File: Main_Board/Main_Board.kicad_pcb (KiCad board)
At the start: 2 copper layers, 99 x 70 mm, 28 parts, among them J1 DB25, P1 CONN_01X08, P2 CONN_01X08, P3 CONN_01X03, U1 TLV1117LV33, U2 DYS_mini_ESC, U3 DYS_mini_ESC, U4 DYS_mini_ESC, U5 DYS_mini_ESC, U6 TENDA_P200, U7 AL8805W5

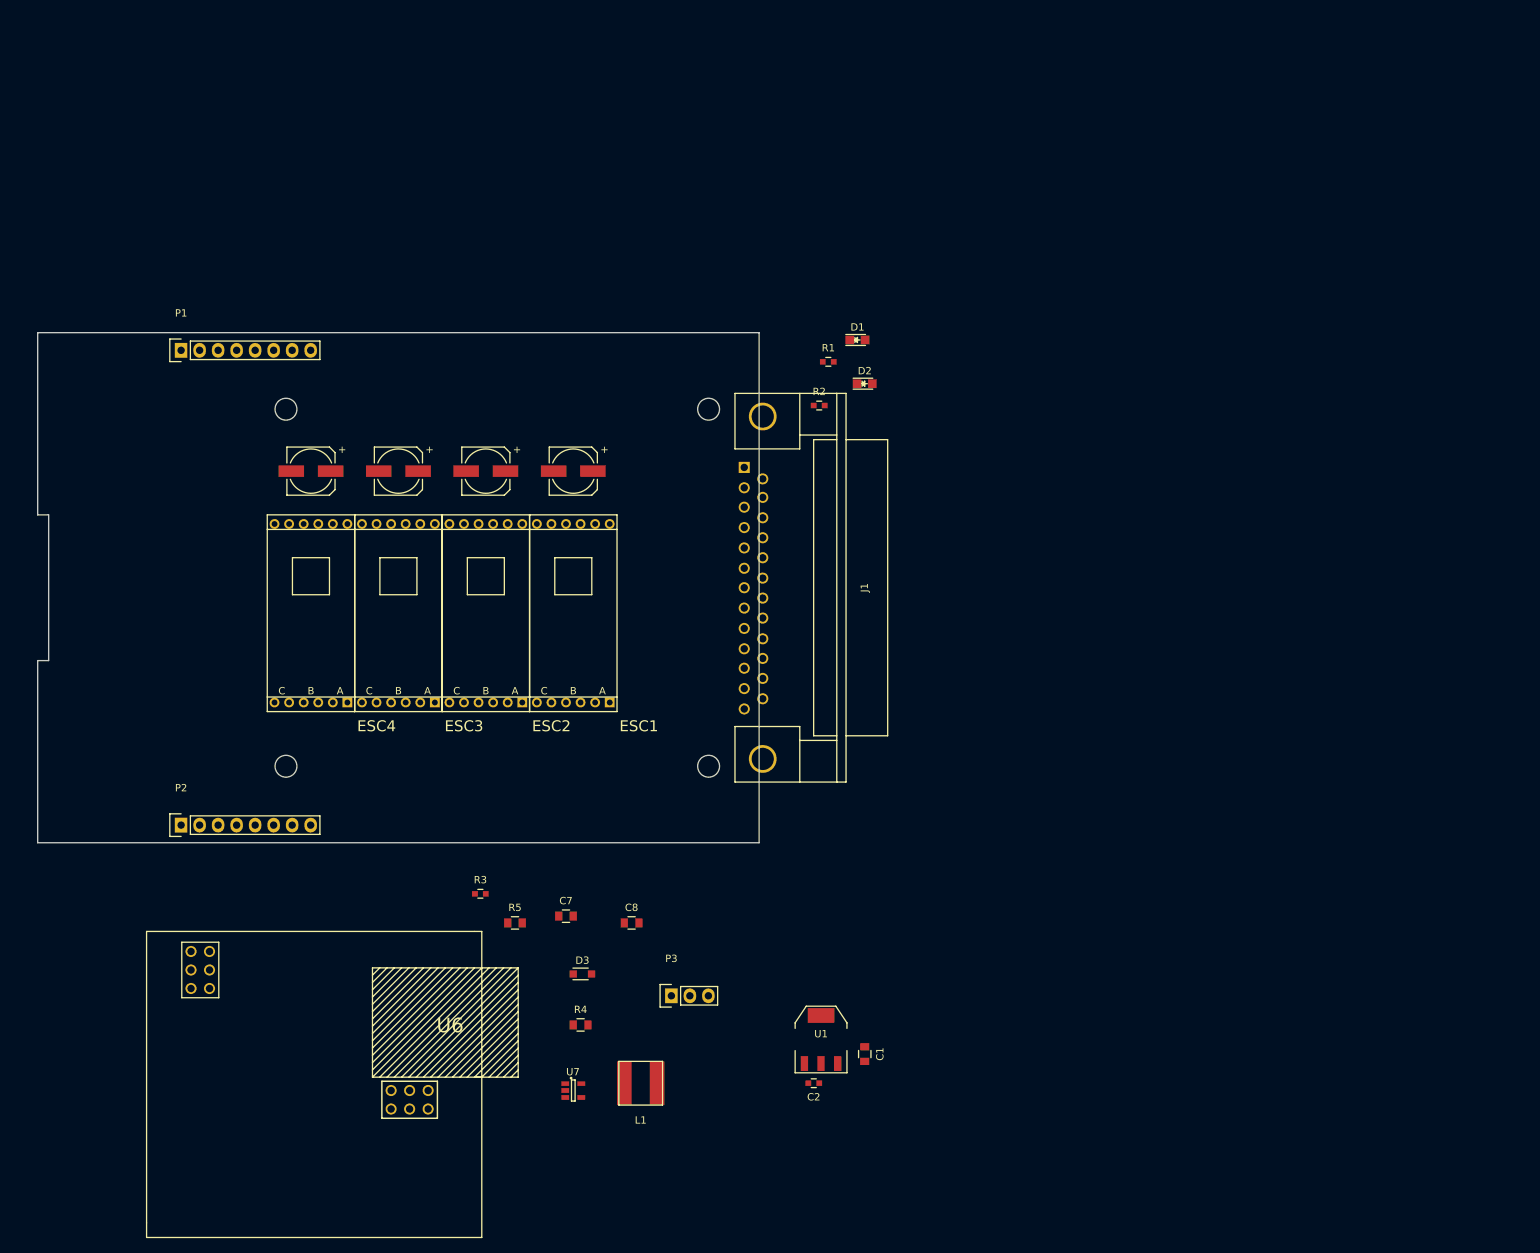
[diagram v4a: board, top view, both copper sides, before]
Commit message: Main Board : Recover LED driver USB Dist Board : Delete ADC voltage divider
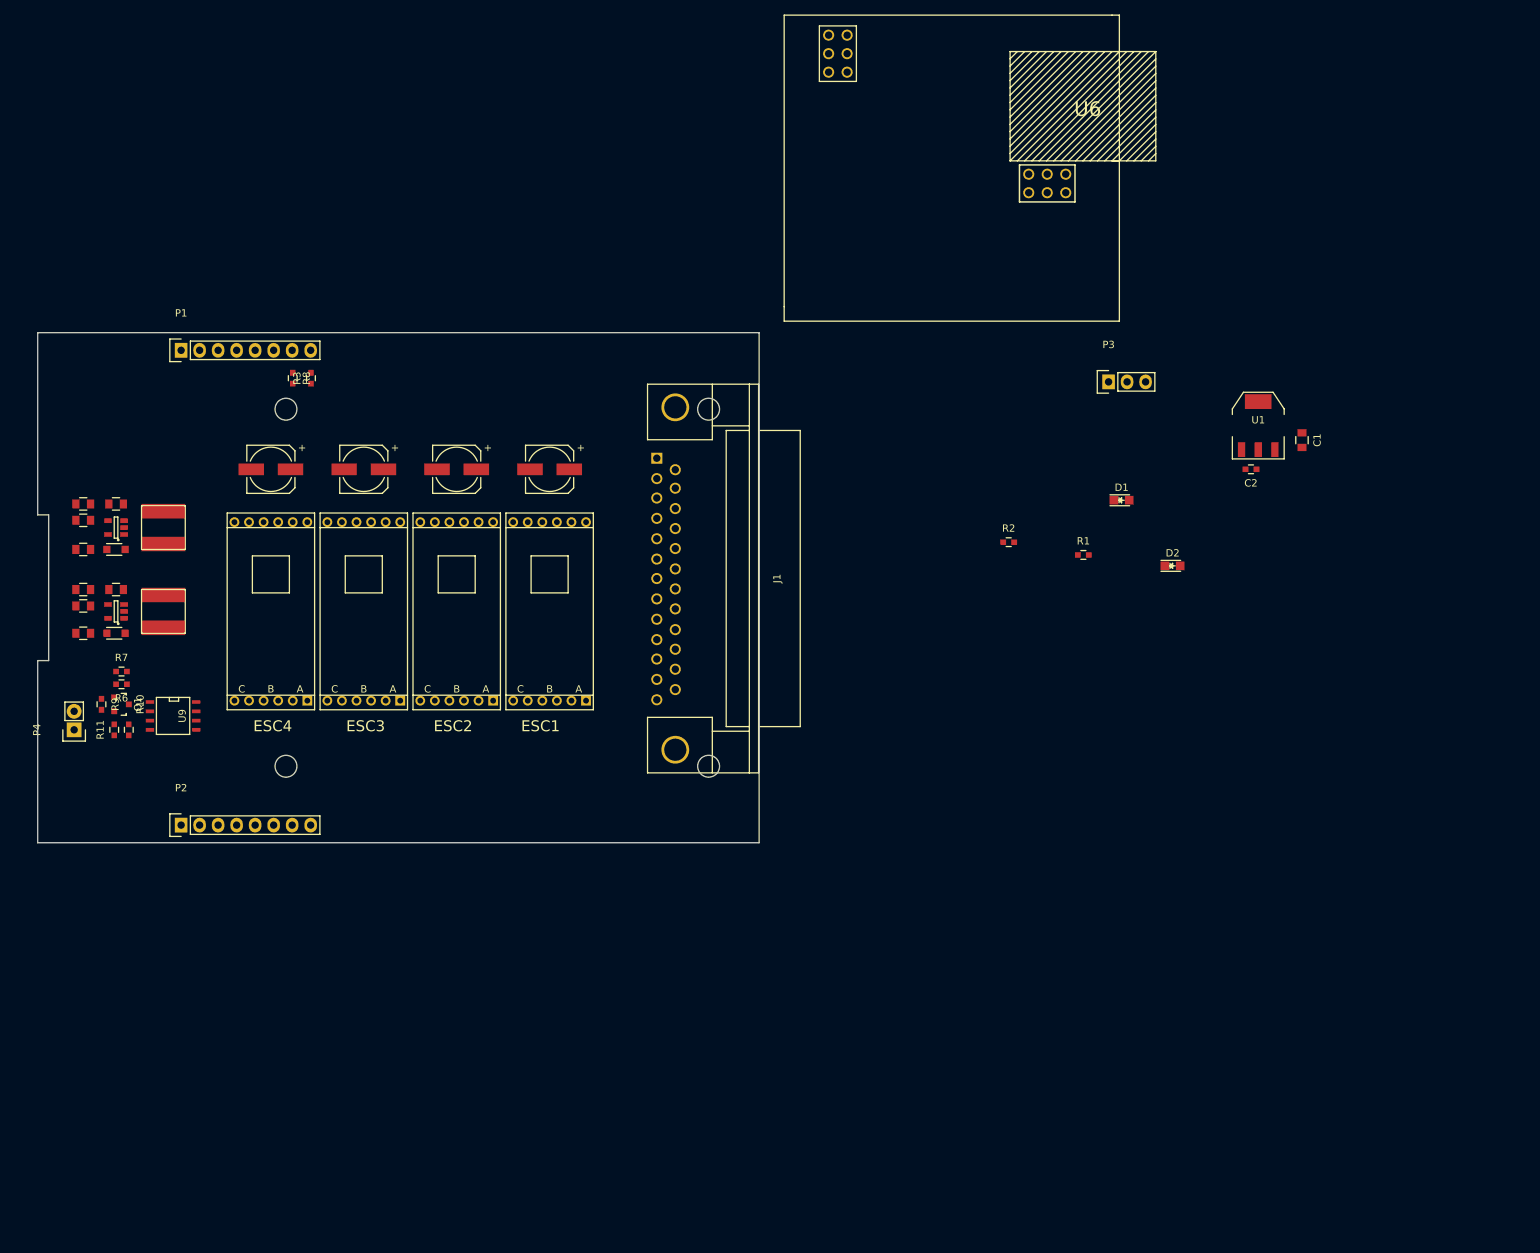
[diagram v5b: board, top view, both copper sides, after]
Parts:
- added C10: 2.2uF, Capacitors_SMD:C_0805, F.Cu at (56.8, 106.2)
- added C9: 1uF, Capacitors_SMD:C_0805, F.Cu at (61.2, 100.2)
- added D4: BAT20JFILM, Diodes_SMD:SOD-323_HandSoldering, F.Cu at (61.2, 106.2)
- added L2: 33uH, KiCad_Footprint:inductor_33uH, F.Cu at (67.8, 103.2)
- added P4: CONN_01X02, Socket_Strips:Socket_Strip_Straight_1x02, F.Cu at (55.5, 119.5)
- added Q1: DMN65D8L, TO_SOT_Packages_SMD:SOT-23, F.Cu at (62.0, 116.0)
- added R10: 10k, Capacitors_SMD:C_0603, F.Cu at (63.0, 119.5)
- added R11: 1k, Capacitors_SMD:C_0603, F.Cu at (61.0, 119.5)
- added R12: 0.5, Capacitors_SMD:C_0805, F.Cu at (56.8, 102.5)
- added R13: 0.5, Capacitors_SMD:C_0805, F.Cu at (56.8, 100.2)
- added R6: 20k 1%, Capacitors_SMD:C_0603, F.Cu at (62.0, 113.2)
- added R7: 102k 1%, Capacitors_SMD:C_0603, F.Cu at (62.0, 111.5)
- added R8: 10k, Capacitors_SMD:C_0603, F.Cu at (85.5, 71.2)
- added R9: 10k, Capacitors_SMD:C_0603, F.Cu at (59.2, 116.0)
- added U8: AL8805W5, TO_SOT_Packages_SMD:SOT-23-5, F.Cu at (61.2, 103.2)
- added U9: SI4425DDY, SMD_Packages:SOIC-8-N, F.Cu at (69.1, 117.6)
- moved U6 153.2 mm to (175.4, 42.4)
- moved C1 103.4 mm to (224.0, 79.8)
- moved C2 103.4 mm to (217.0, 83.8)
- moved P3 103.4 mm to (197.5, 71.8)
- moved U1 103.4 mm to (218.0, 77.8)
- moved L1 100.5 mm to (67.8, 91.8), turned to 90 degrees
- moved U7 99.5 mm to (61.2, 91.8), turned to 180 degrees
- moved R4 98.8 mm to (56.8, 88.5)
- moved C8 91.0 mm to (56.8, 94.8), turned to 180 degrees
- moved D3 86.5 mm to (61.2, 94.8)
- moved C7 83.7 mm to (61.2, 88.5)
- moved R5 81.0 mm to (56.8, 90.8)
- moved R3 74.5 mm to (88.0, 71.2), turned to 90 degrees
- moved D2 49.1 mm to (206.2, 97.0)
- moved R1 43.9 mm to (194.0, 95.5)
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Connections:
- net /Bottom_Board/LED+ renamed /Bottom_Board/LED1+
- net /Bottom_Board/LED- renamed /Bottom_Board/LED1-
- C3 pad 1: /Bottom_Board/V_BAT -> /Bottom_Board/V_PWR
- C4 pad 1: /Bottom_Board/V_BAT -> /Bottom_Board/V_PWR
- C5 pad 1: /Bottom_Board/V_BAT -> /Bottom_Board/V_PWR
- C6 pad 1: /Bottom_Board/V_BAT -> /Bottom_Board/V_PWR
- C8 pad 1: /Bottom_Board/V_BAT -> /Bottom_Board/V_PWR
- D3 pad 1: /Bottom_Board/V_BAT -> /Bottom_Board/V_PWR
- P1 pad 7: (no net) -> /Bottom_Board/CH6
- P2 pad 1: (no net) -> /Bottom_Board/ADC
- P2 pad 6: (no net) -> /Bottom_Board/SW
- R4 pad 1: /Bottom_Board/V_BAT -> /Bottom_Board/V_PWR
- R5 pad 1: /Bottom_Board/V_BAT -> /Bottom_Board/V_PWR
- U2 pad 3: /Bottom_Board/V_BAT -> /Bottom_Board/V_PWR
- U3 pad 3: /Bottom_Board/V_BAT -> /Bottom_Board/V_PWR
- U4 pad 3: /Bottom_Board/V_BAT -> /Bottom_Board/V_PWR
- U5 pad 3: /Bottom_Board/V_BAT -> /Bottom_Board/V_PWR
- U7 pad 5: /Bottom_Board/V_BAT -> /Bottom_Board/V_PWR

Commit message: development start
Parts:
- added C11: C, Capacitors_SMD:C_0805, F.Cu at (123.6, 131.9)
- added C12: C, Capacitors_SMD:C_0603, F.Cu at (125.8, 129.8)
- added P5: CONN_01X02, Socket_Strips:Socket_Strip_Straight_1x02, F.Cu at (119.6, 130.0)
- added R14: 10k, Capacitors_SMD:C_0603, B.Cu at (77.8, 70.9)
- added R15: 10k, Capacitors_SMD:C_0603, B.Cu at (75.3, 70.9)
- added R16: 10k, Capacitors_SMD:C_0603, B.Cu at (82.9, 70.9)
- added R17: 10k, Capacitors_SMD:C_0603, B.Cu at (80.4, 70.9)
- added U10: DSN-MINI-360, KiCad_Footprint:DSN-MINI-360, F.Cu at (106.7, 127.6)
- added U11: TLV1117LV33, TO_SOT_Packages_SMD:SOT-223, F.Cu at (131.6, 130.8)
- R3, R8: moved to B.Cu
- moved U2 2.00 mm to (120.8, 101.2)
- moved U3 2.00 mm to (108.0, 101.2)
- moved U4 2.00 mm to (95.2, 101.2)
- moved U5 2.00 mm to (82.5, 101.2)
- moved J1 1.26 mm to (136.7, 100.0)
- moved C3 1.00 mm to (120.8, 82.8)
- moved C4 1.00 mm to (108.0, 82.8)
- moved C5 1.00 mm to (95.2, 82.8)
- moved C6 1.00 mm to (82.5, 82.8)
- moved R3 0.35 mm to (88.0, 70.9)
- moved R8 0.35 mm to (85.5, 70.9)
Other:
- net class Default: trace_width 0.25 -> 2

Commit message: shit
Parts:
- added C13: 33uF, Capacitors_SMD:C_0603, F.Cu at (70.4, 99.5)
- added C14: 33uF, Capacitors_SMD:C_0603, F.Cu at (73.5, 99.5)
- added C15: 1uF, Capacitors_SMD:C_0603, B.Cu at (70.2, 108.8)
- added C16: 1uF, Capacitors_SMD:C_0603, B.Cu at (70.2, 105.7)
- added C17: 1uF, Capacitors_SMD:C_0603, B.Cu at (72.8, 108.8)
- added C18: 1uF, Capacitors_SMD:C_0603, B.Cu at (72.8, 105.7)
- added C19: 47pF, Capacitors_SMD:C_0603, F.Cu at (70.7, 114.8)
- added C20: 47pF, Capacitors_SMD:C_0603, F.Cu at (73.9, 114.8)
- added C21: 10uF, Capacitors_SMD:C_0603, F.Cu at (65.1, 95.2)
- added D5: LED, LEDs:LED_0805, F.Cu at (200.7, 154.0)
- added P10: CONN_01X02, Socket_Strips:Socket_Strip_Straight_1x02, F.Cu at (127.7, 76.5)
- added P11: CONN_01X02, Socket_Strips:Socket_Strip_Straight_1x02, F.Cu at (129.2, 123.5)
- added P12: CONN_01X02, Socket_Strips:Socket_Strip_Straight_1x02, F.Cu at (88.7, 123.5)
- added P13: CONN_02X07, Socket_Strips:Socket_Strip_Straight_2x07, F.Cu at (64.8, 123.2)
- added P14: USB_A, Connect:USB_Mini-B, F.Cu at (56.2, 130.4)
- added P6: BOOT, Socket_Strips:Socket_Strip_Straight_1x02, F.Cu at (214.2, 155.8)
- added P7: CONN_01X06, Socket_Strips:Socket_Strip_Straight_1x06, F.Cu at (53.5, 83.6)
- added P8: CONN_01X04, Socket_Strips:Socket_Strip_Angled_1x04, F.Cu at (57.5, 112.7)
- added P9: CONN_01X02, Socket_Strips:Socket_Strip_Straight_1x02, F.Cu at (89.5, 76.5)
- added Q2: BSS84, TO_SOT_Packages_SMD:SOT-23, F.Cu at (77.5, 117.5)
- added Q3: BSS138, TO_SOT_Packages_SMD:SOT-23, F.Cu at (60.3, 107.2)
- added Q4: BSS138, TO_SOT_Packages_SMD:SOT-23, F.Cu at (60.3, 103.8)
- added R18: 330, Capacitors_SMD:C_0603, F.Cu at (198.7, 154.1)
- added R19: 10k, Capacitors_SMD:C_0603, F.Cu at (205.5, 149.6)
- added R20: 10k, Capacitors_SMD:C_0603, F.Cu at (208.2, 156.6)
- added R21: 10k, Capacitors_SMD:C_0603, F.Cu at (77.5, 114.8)
- added R22: 1.5k, Capacitors_SMD:C_0603, F.Cu at (74.8, 117.5)
- added R23: 22, Capacitors_SMD:C_0603, F.Cu at (71.5, 117.5)
- added R24: 22, Capacitors_SMD:C_0603, F.Cu at (73.2, 117.5)
- added RP1: 220X4, Resistors_SMD:R_Array_Concave_4x0603, F.Cu at (58.4, 88.3)
- added RP2: 220X4, Resistors_SMD:R_Array_Concave_4x0603, F.Cu at (54.6, 88.2)
- added RP3: 220X4, Resistors_SMD:R_Array_Concave_4x0603, F.Cu at (55.0, 100.0)
- added SW1: RESET, KiCad_Footprint:smd_push, F.Cu at (214.9, 148.9)
- added U12: STM32F103CBT6, Housings_QFP:LQFP-48_7x7mm_Pitch0.5mm, F.Cu at (71.4, 107.3)
- added U13: pca9685, Housings_SSOP:TSSOP-28_4.4x9.7mm_Pitch0.65mm, F.Cu at (58.1, 93.9)
- added X1: 8MHz, KiCad_Footprint:crystal_maple, F.Cu at (72.0, 96.5)
- P1, P2: value CONN_01X08 -> CONN_01X06; footprint Socket_Strips:Socket_Strip_Straight_1x08 -> Socket_Strips:Socket_Strip_Straight_1x06
- R14, R15, R16, R17, R3, R8: moved to F.Cu
- moved P4 79.8 mm to (117.0, 68.7), turned to 270 degrees
- moved U6 75.0 mm to (221.5, 101.5)
- moved R11 71.6 mm to (111.5, 68.7), turned to 270 degrees
- moved R9 69.5 mm to (113.2, 72.2), turned to 90 degrees
- moved R10 68.9 mm to (109.5, 68.7), turned to 90 degrees
- moved Q1 65.3 mm to (110.4, 72.2), turned to 90 degrees
- moved R6 61.8 mm to (110.5, 74.9), turned to 0 degrees
- moved R7 59.7 mm to (110.5, 76.7), turned to 180 degrees
- moved U9 58.2 mm to (103.4, 70.6), turned to 90 degrees
- moved P2 50.9 mm to (56.4, 83.6), turned to 90 degrees
- moved C1 47.7 mm to (251.5, 40.8)
- moved C2 47.7 mm to (244.5, 44.8)
- moved D1 47.7 mm to (226.8, 49.0)
- moved D2 47.7 mm to (233.8, 58.0)
- moved R1 47.7 mm to (221.5, 56.5)
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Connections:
- C10 pad 2: /Bottom_Board/L_GND -> GNDPWR
- C11 pad 2: GND -> GNDD
- C12 pad 2: GND -> GNDD
- C3 pad 2: /Bottom_Board/L_GND -> GNDPWR
- C4 pad 2: /Bottom_Board/L_GND -> GNDPWR
- C5 pad 2: /Bottom_Board/L_GND -> GNDPWR
- C6 pad 2: /Bottom_Board/L_GND -> GNDPWR
- C8 pad 2: /Bottom_Board/L_GND -> GNDPWR
- P1 pad 1: /Bottom_Board/V_BAT -> Net-(P1-Pad1)
- P1 pad 2: /Bottom_Board/L_GND -> Net-(P1-Pad2)
- P1 pad 3: /Bottom_Board/CH2 -> Net-(P1-Pad3)
- P1 pad 4: /Bottom_Board/CH1 -> Net-(P1-Pad4)
- P1 pad 5: /Bottom_Board/CH4 -> Net-(P1-Pad5)
- P1 pad 6: /Bottom_Board/CH3 -> Net-(P1-Pad6)
- P2 pad 1: /Bottom_Board/ADC -> /Bottom_Board/5V
- P2 pad 2: /Bottom_Board/L_GND -> /Bottom_Board/5V
- P2 pad 3: (no net) -> /Bottom_Board/5V
- P2 pad 4: (no net) -> /Bottom_Board/5V
- P2 pad 5: (no net) -> /Bottom_Board/5V
- P2 pad 6: /Bottom_Board/SW -> /Bottom_Board/5V
- P4 pad 2: /Bottom_Board/L_GND -> GNDD
- P5 pad 1: /Bottom_Board/L_GND -> GNDD
- Q1 pad 2: /Bottom_Board/L_GND -> GNDD
- R14 pad 1: /Bottom_Board/CH1 -> /Bottom_Board/3V3
- R14 pad 2: /Bottom_Board/L_GND -> /Bottom_Board/SDA_3V3
- R15 pad 1: /Bottom_Board/CH2 -> /Bottom_Board/5V
- R15 pad 2: /Bottom_Board/L_GND -> /Bottom_Board/SDA_5V
- R16 pad 1: /Bottom_Board/CH3 -> /Bottom_Board/3V3
- R16 pad 2: /Bottom_Board/L_GND -> /Bottom_Board/SCL_3V3
- R17 pad 1: /Bottom_Board/CH4 -> /Bottom_Board/5V
- R17 pad 2: /Bottom_Board/L_GND -> /Bottom_Board/SCL_5V
- R3 pad 1: /Bottom_Board/CH5 -> Net-(R3-Pad1)
- R3 pad 2: /Bottom_Board/L_GND -> GNDD
- R7 pad 2: /Bottom_Board/L_GND -> GNDD
- R8 pad 1: /Bottom_Board/CH6 -> Net-(R8-Pad1)
- R8 pad 2: /Bottom_Board/L_GND -> GNDD
- R9 pad 2: /Bottom_Board/L_GND -> GNDD
- U10 pad 2: /Bottom_Board/L_GND -> GNDPWR
- U10 pad 4: /Bottom_Board/L_GND -> GNDD
- U11 pad 1: GND -> GNDD
- U2 pad 1: /Bottom_Board/L_GND -> GNDPWR
- U3 pad 1: /Bottom_Board/L_GND -> GNDPWR
- U4 pad 1: /Bottom_Board/L_GND -> GNDPWR
- U5 pad 1: /Bottom_Board/L_GND -> GNDPWR
- U7 pad 2: /Bottom_Board/L_GND -> GNDPWR
- U8 pad 2: /Bottom_Board/L_GND -> GNDPWR
